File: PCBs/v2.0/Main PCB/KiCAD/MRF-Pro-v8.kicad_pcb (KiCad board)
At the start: 2 copper layers, 56.5 x 28.7 mm, 6 parts, among them J1 Feather-1, J2 Feather-2, J3 FPC 8P Connector, J4 Conn_01x08

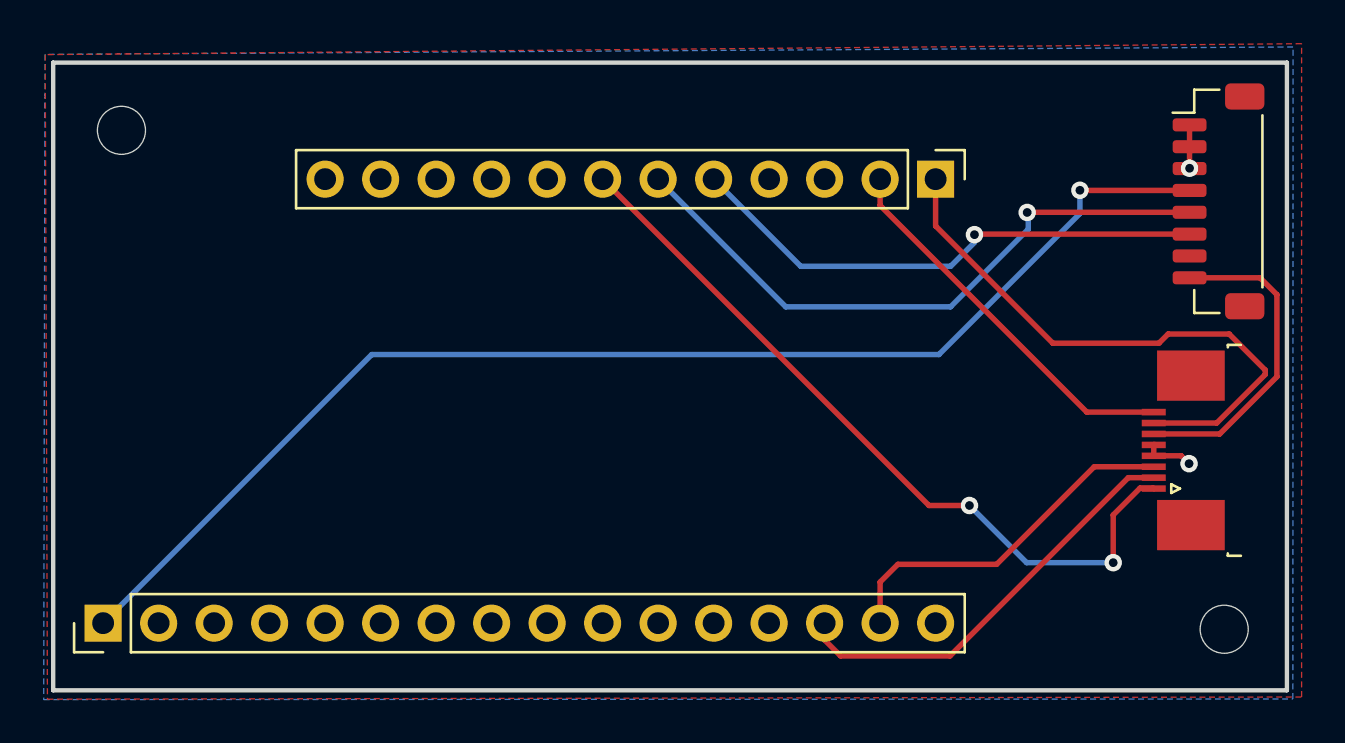
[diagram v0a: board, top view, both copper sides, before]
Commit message: Rework the main-board power switch as a J4 DPDT and lay out the board
The power switch moves onto the 8-pin J4 header as a DPDT: pole A
gates the Feather 3.3V onto the switched rail 3V3_SW (FPC pin 1),
pole B pulls Feather EN to GND when off, holding the MCU off. This
fixes the prior topology where FPC pin 1 ran from a GPIO (D11) and the
Feather 3.3V never reached the FPC. Feather BAT now drives VBAT to FPC
pin 6 for the breakout LDO. Routed to match; D11 and RST are freed.
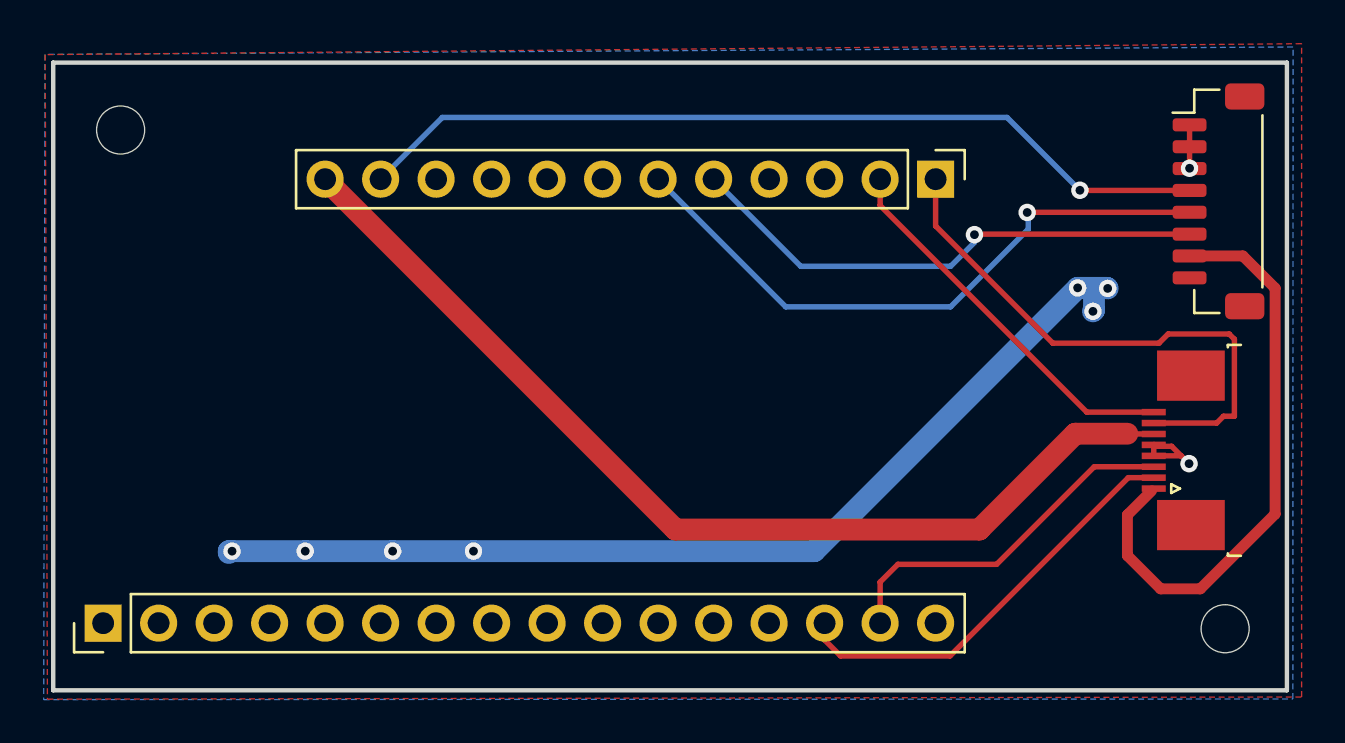
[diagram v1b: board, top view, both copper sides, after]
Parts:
- removed the REF** at (159.3, 122.2)
- removed the REF** at (108.8, 99.4)
- added REF**: MountingHole_2.2mm_M2, MountingHole:MountingHole_2.2mm_M2, F.Cu at (108.8, 99.3)
- added REF**: MountingHole_2.2mm_M2, MountingHole:MountingHole_2.2mm_M2, F.Cu at (159.3, 122.2)
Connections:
- J1 pad 1: Net-(J1-Pin_1) -> unconnected-(J1-Pin_1-Pad1)
- J2 pad 11: unconnected-(J2-Pin_11-Pad11) -> /EN
- J2 pad 12: unconnected-(J2-Pin_12-Pad12) -> /VBAT
- J2 pad 7: Net-(J2-Pin_7) -> unconnected-(J2-Pin_7-Pad7)
- J3 pad 1: Net-(J2-Pin_7) -> /3V3_SW
- J3 pad 6: Net-(J3-Pin_6) -> /VBAT
- J4 pad 4: Net-(J1-Pin_1) -> /EN
- J4 pad 7: /3.3V -> /3V3_SW
- J4 pad 8: Net-(J3-Pin_6) -> /3.3V
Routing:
- net Net-(J1-Pin_1): track 58.6 -> 0.00 mm, vias 1 -> 0
- net /3.3V: track 0.15 -> 46.6 mm, vias 0 -> 7
- net /VBAT: track 0.00 -> 46.4 mm
- net /EN: track 0.00 -> 39.6 mm, vias 0 -> 1
- net Net-(J2-Pin_7): track 35.2 -> 0.00 mm, vias 2 -> 0
- net /3V3_SW: track 0.00 -> 27.1 mm
- net Net-(J3-Pin_6): track 14.8 -> 0.00 mm
- net /GND: track 4.30 -> 5.74 mm
- net Net-(J2-Pin_1): track 26.6 -> 25.8 mm
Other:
- board text added: "MRF2 Daughterboard v8"
- board text removed: "MRF2 Daughterboard v7.5"

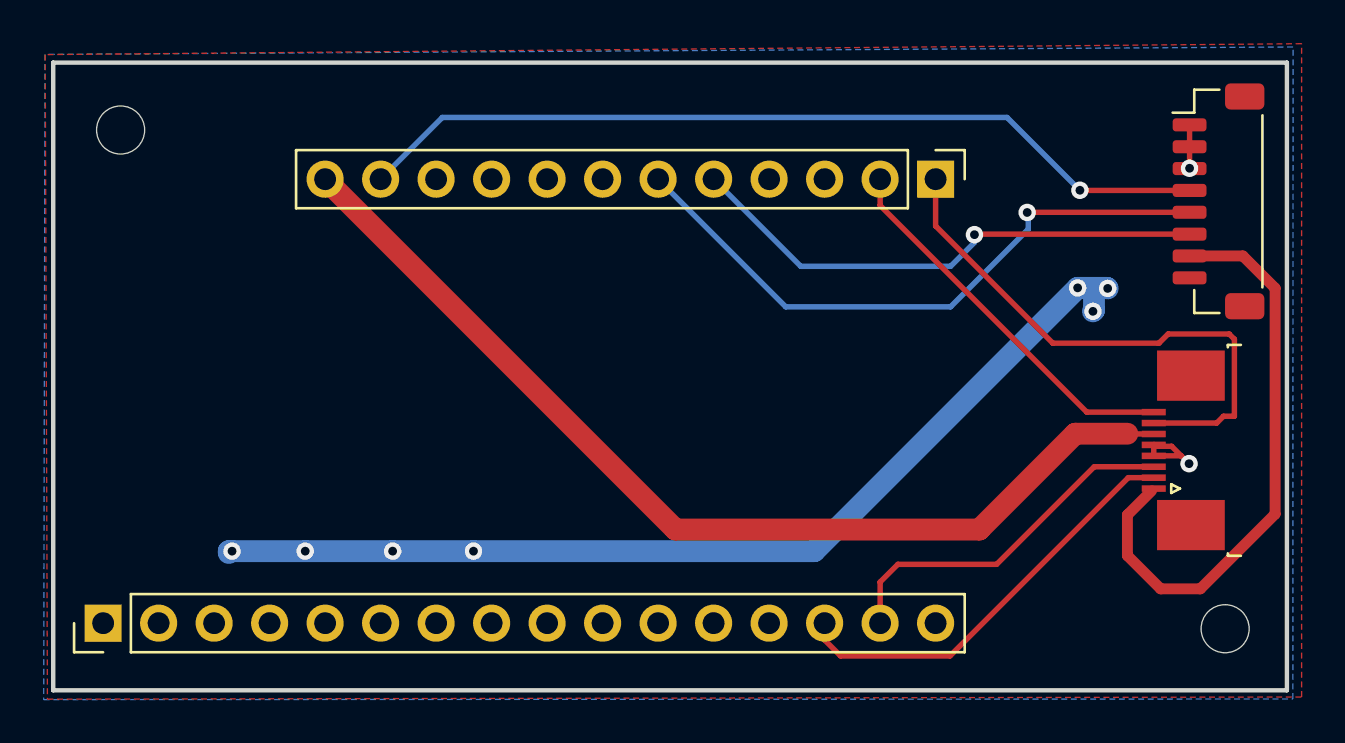
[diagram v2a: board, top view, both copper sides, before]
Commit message: Swap FPC pins 1 and 6, reroute both boards, re-plot fab
VBAT now lands on FPC pin 1 (beside the UART pair) and the switched 3.3 V
on pin 6 (beside the I2C pair), so the always-on battery rail no longer
runs next to the I2C lines. Both boards' schematics were tidied up and
fully rerouted; DRC passes clean on each. Gerbers and the JLCPCB position
files are re-plotted to match. The BOM is unchanged - this is a net and
placement change, not a parts change.
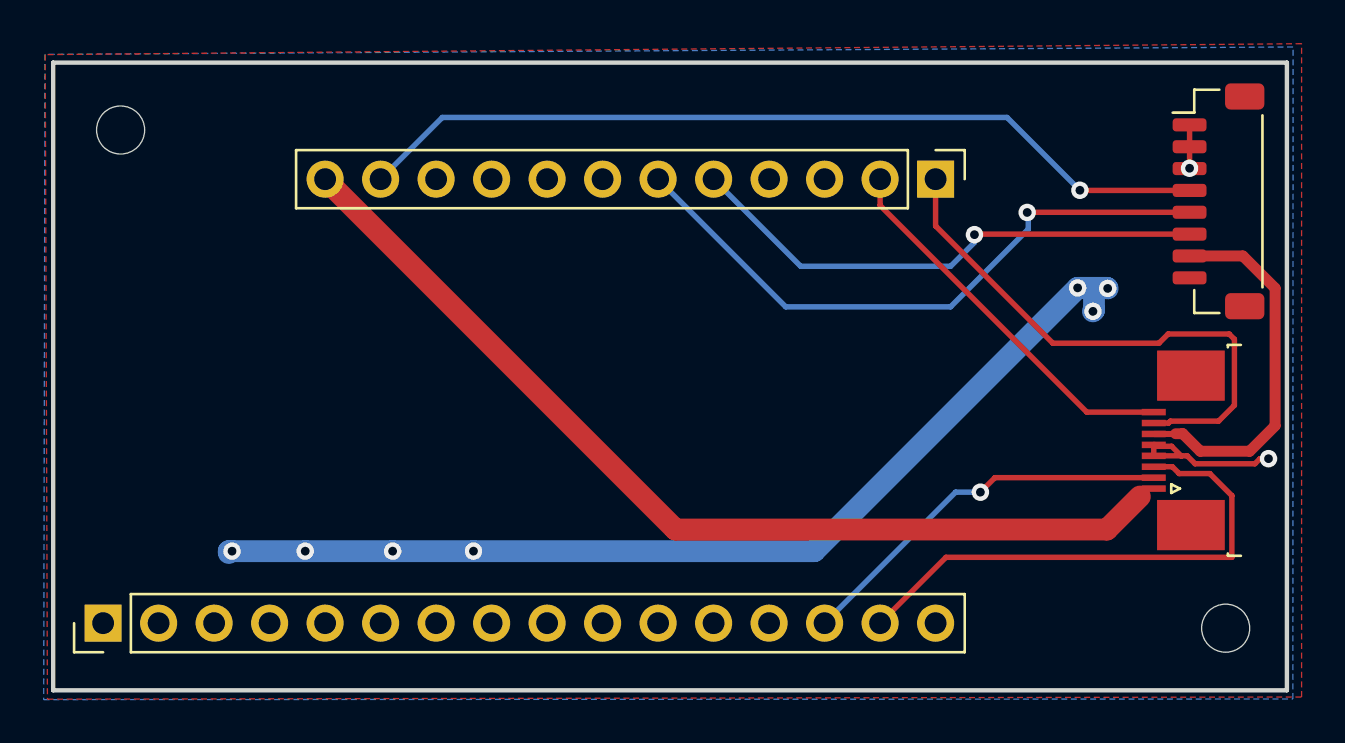
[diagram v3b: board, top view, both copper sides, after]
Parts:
- removed REF** (x2): MountingHole_2.2mm_M2, MountingHole:MountingHole_2.2mm_M2
- added H1: MountingHole, MountingHole:MountingHole_2.2mm_M2, F.Cu at (159.3, 122.2)
- added H2: MountingHole, MountingHole:MountingHole_2.2mm_M2, F.Cu at (108.8, 99.3)
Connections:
- J3 pad 1: /3V3_SW -> /VBAT
- J3 pad 6: /VBAT -> /3V3_SW
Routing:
- net /3V3_SW: track 27.1 -> 17.2 mm
- net Net-(J1-Pin_15): track 16.6 -> 24.3 mm
- net /GND: track 5.74 -> 9.47 mm
- net /VBAT: track 46.4 -> 44.6 mm
- net Net-(J1-Pin_14): track 19.5 -> 17.8 mm, vias 0 -> 1
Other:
- board text added: "SCL SDA 3.3V GND GND RX TX VBAT"
- board text removed: "SCL SDA V+ GND GND RX TX PWM"
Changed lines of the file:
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@@
 	(footprint "MountingHole:MountingHole_2.2mm_M2"
 		(layer "F.Cu")
-		(at 108.75 99.35)
+		(at 159.325 122.15)
 		(descr "Mounting Hole 2.2mm, M2, no annular, generated by kicad-footprint-generator mountinghole.py")
 		(tags "mountinghole M2")
-		(property "Reference" "REF**"
+		(property "Reference" "H1"
 			(at 0 -3.15 0)
 			(layer "F.SilkS")
@@
 			)
 		)
-		(property "Value" "MountingHole_2.2mm_M2"
+		(property "Value" "MountingHole"
 			(at 0 3.15 0)
 			(layer "F.Fab")
@@
 			)
 		)
-		(property "Description" ""
+		(property "Description" "Mounting Hole without connection"
 			(at 0 0 0)
 			(layer "F.Fab")
@@
 			)
 		)
-		(attr exclude_from_pos_files exclude_from_bom)
+		(property ki_fp_filters "MountingHole*")
+		(sheetname "/")
+		(sheetfile "MRF-Pro-v8.kicad_sch")
+		(units
+			(unit
+				(name "A")
+				(pins)
+			)
+		)
+		(attr exclude_from_bom)
 		(duplicate_pad_numbers_are_jumpers no)
 		(fp_circle
@@
 	(footprint "MountingHole:MountingHole_2.2mm_M2"
 		(layer "F.Cu")
-		(at 159.3 122.175)
+		(at 108.75 99.35)
 		(descr "Mounting Hole 2.2mm, M2, no annular, generated by kicad-footprint-generator mountinghole.py")
 		(tags "mountinghole M2")
-		(property "Reference" "REF**"
+		(property "Reference" "H2"
 			(at 0 -3.15 0)
 			(layer "F.SilkS")
@@
 			)
 		)
-		(property "Value" "MountingHole_2.2mm_M2"
+		(property "Value" "MountingHole"
 			(at 0 3.15 0)
 			(layer "F.Fab")
@@
 			)
 		)
-		(property "Description" ""
+		(property "Description" "Mounting Hole without connection"
 			(at 0 0 0)
 			(layer "F.Fab")
@@
 			)
 		)
-		(attr exclude_from_pos_files exclude_from_bom)
+		(property ki_fp_filters "MountingHole*")
+		(sheetname "/")
+		(sheetfile "MRF-Pro-v8.kicad_sch")
+		(units
+			(unit
+				(name "A")
+				(pins)
+			)
+		)
+		(attr exclude_from_bom)
 		(duplicate_pad_numbers_are_jumpers no)
 		(fp_circle
@@
 			(size 0.3 1.1)
 			(layers "F.Cu" "F.Mask" "F.Paste")
-			(net "/3V3_SW")
+			(net "/VBAT")
 			(pinfunction "Pin_1_1")
 			(pintype "passive")
@@
 			(size 0.3 1.1)
 			(layers "F.Cu" "F.Mask" "F.Paste")
-			(net "/VBAT")
+			(net "/3V3_SW")
 			(pinfunction "Pin_6_6")
 			(pintype "passive")
@@
 		(layer "Edge.Cuts")
 	)
-	(gr_text "SCL\nSDA\nV+\nGND\nGND\nRX\nTX\nPWM"
+	(gr_text "SCL\nSDA\n3.3V\nGND\nGND\nRX\nTX\nVBAT"
 		(at 154.6606 118.618 0)
 		(layer "B.SilkS")
@@
 	)
 	(segment
-		(start 158.914 112.7616)
-		(end 159.2256 112.45)
-		(width 0.25)
-		(layer "F.Cu")
-		(net "Net-(J2-Pin_1)")
-	)
-	(segment
 		(start 156.2724 109.1068)
 		(end 156.6926 108.6866)
@@
 	)
 	(segment
-		(start 158.914 112.7616)
-		(end 156.034 112.7616)
-		(width 0.25)
-		(layer "F.Cu")
-		(net "Net-(J2-Pin_1)")
-	)
-	(segment
 		(start 159.725 108.925)
 		(end 159.4866 108.6866)
@@
 	)
 	(segment
-		(start 159.2256 112.45)
-		(end 159.725 112.45)
+		(start 156.709227 112.7616)
+		(end 156.034 112.7616)
 		(width 0.25)
 		(layer "F.Cu")
@@
 	)
 	(segment
-		(start 159.725 112.45)
-		(end 159.725 108.925)
+		(start 159.0006 112.675)
+		(end 156.795827 112.675)
 		(width 0.25)
 		(layer "F.Cu")
@@
 	)
 	(segment
+		(start 159.725 108.925)
+		(end 159.725 111.9506)
+		(width 0.25)
+		(layer "F.Cu")
+		(net "Net-(J2-Pin_1)")
+	)
+	(segment
 		(start 146.05 103.742905)
 		(end 151.413895 109.1068)
@@
 	)
 	(segment
+		(start 159.725 111.9506)
+		(end 159.0006 112.675)
+		(width 0.25)
+		(layer "F.Cu")
+		(net "Net-(J2-Pin_1)")
+	)
+	(segment
 		(start 156.6926 108.6866)
 		(end 159.4866 108.6866)
+		(width 0.25)
+		(layer "F.Cu")
+		(net "Net-(J2-Pin_1)")
+	)
+	(segment
+		(start 156.795827 112.675)
+		(end 156.709227 112.7616)
 		(width 0.25)
 		(layer "F.Cu")
@@
 	)
 	(segment
-		(start 154.825 113.25)
-		(end 152.440235 113.25)
+		(start 134.1452 117.6352)
+		(end 153.8898 117.6352)
 		(width 1)
 		(layer "F.Cu")
@@
 	)
 	(segment
-		(start 156.034 113.2616)
-		(end 154.8366 113.2616)
-		(width 0.25)
+		(start 153.8898 117.6352)
+		(end 155.4 116.125)
+		(width 1)
 		(layer "F.Cu")
 		(net "/VBAT")
 	)
 	(segment
-		(start 156.0224 113.25)
-		(end 156.034 113.2616)
-		(width 0.25)
-		(layer "F.Cu")
-		(net "/VBAT")
-	)
-	(segment
-		(start 134.1452 117.6352)
-		(end 118.11 101.6)
-		(width 1)
-		(layer "F.Cu")
-		(net "/VBAT")
-	)
-	(segment
-		(start 154.8366 113.2616)
-		(end 154.825 113.25)
-		(width 0.25)
-		(layer "F.Cu")
-		(net "/VBAT")
-	)
-	(segment
-		(start 148.055035 117.6352)
+		(start 118.11 101.6)
 		(end 134.1452 117.6352)
 		(width 1)
@@
 	)
 	(segment
-		(start 152.440235 113.25)
-		(end 148.055035 117.6352)
-		(width 1)
-		(layer "F.Cu")
-		(net "/VBAT")
+		(start 160.896454 114.391719)
+		(end 160.663172 114.625)
+		(width 0.25)
+		(layer "F.Cu")
+		(net "/GND")
+	)
+	(segment
+		(start 157.5616 114.2616)
+		(end 157.2916 114.2616)
+		(width 0.25)
+		(layer "F.Cu")
+		(net "/GND")
 	)
 	(segment
@@
 	)
 	(segment
-		(start 157.65 114.62)
-		(end 157.2916 114.2616)
+		(start 160.663172 114.625)
+		(end 157.924999 114.625)
+		(width 0.25)
+		(layer "F.Cu")
+		(net "/GND")
+	)
+	(segment
+		(start 157.924999 114.625)
+		(end 157.5616 114.2616)
+		(width 0.25)
+		(layer "F.Cu")
+		(net "/GND")
+	)
+	(segment
+		(start 161.285364 114.391719)
+		(end 160.896454 114.391719)
 		(width 0.25)
 		(layer "F.Cu")
@@
 	)
 	(via
-		(at 157.65 114.62)
+		(at 161.285364 114.391719)
 		(size 0.8)
 		(drill 0.4)
@@
 	)
 	(segment
-		(start 154.8286 118.8286)
-		(end 156.35 120.35)
+		(start 156.034 113.2616)
+		(end 157.0224 113.2616)
+		(width 0.28)
+		(layer "F.Cu")
+		(net "/3V3_SW")
+	)
+	(segment
+		(start 160.425 114.05)
+		(end 158.163172 114.05)
 		(width 0.5)
 		(layer "F.Cu")
@@
 	)
 	(segment
-		(start 154.8286 116.967)
-		(end 154.8286 118.8286)
+		(start 156.0224 113.25)
+		(end 156.034 113.2616)
+		(width 0.25)
+		(layer "F.Cu")
+		(net "/3V3_SW")
+	)
+	(segment
+		(start 161.5876 112.8874)
+		(end 160.425 114.05)
 		(width 0.5)
 		(layer "F.Cu")
@@
 	)
 	(segment
-		(start 161.5876 116.928)
-		(end 161.5876 106.5876)
+		(start 158.163172 114.05)
+		(end 157.363173 113.25)
 		(width 0.5)
 		(layer "F.Cu")
@@
 	)
 	(segment
-		(start 160.1154 105.1154)
-		(end 157.6728 105.1154)
+		(start 157.0224 113.2616)
+		(end 157.034 113.25)
+		(width 0.25)
+		(layer "F.Cu")
+		(net "/3V3_SW")
+	)
+	(segment
+		(start 157.363173 113.25)
+		(end 157.034 113.25)
 		(width 0.5)
 		(layer "F.Cu")
@@
 	)
 	(segment
-		(start 161.5876 106.5876)
+		(start 157.6728 105.1154)
 		(end 160.1154 105.1154)
 		(width 0.5)
@@
 	)
 	(segment
-		(start 156.35 120.35)
-		(end 158.1656 120.35)
+		(start 161.5876 106.5876)
+		(end 161.5876 112.8874)
 		(width 0.5)
 		(layer "F.Cu")
@@
 	)
 	(segment
-		(start 158.1656 120.35)
-		(end 161.5876 116.928)
-		(width 0.5)
-		(layer "F.Cu")
-		(net "/3V3_SW")
-	)
-	(segment
-		(start 155.934 115.8616)
-		(end 154.8286 116.967)
+		(start 160.1154 105.1154)
+		(end 161.5876 106.5876)
 		(width 0.5)
 		(layer "F.Cu")
@@
 	)
 	(segment
-		(start 140.97 122.69)
-		(end 141.7 123.42)
+		(start 148.7634 115.2616)
+		(end 148.1 115.925)
 		(width 0.25)
 		(layer "F.Cu")
@@
 	)
 	(segment
-		(start 140.97 121.92)
-		(end 140.97 122.69)
+		(start 156.034 115.2616)
+		(end 148.7634 115.2616)
 		(width 0.25)
 		(layer "F.Cu")
 		(net "Net-(J1-Pin_14)")
 	)
-	(segment
-		(start 146.709 123.42)
-		(end 154.8674 115.2616)
-		(width 0.25)
-		(layer "F.Cu")
+	(via
+		(at 148.1 115.925)
+		(size 0.8)
+		(drill 0.4)
+		(layers "F.Cu" "B.Cu")
 		(net "Net-(J1-Pin_14)")
 	)
 	(segment
-		(start 141.7 123.42)
-		(end 146.709 123.42)
-		(width 0.25)
-		(layer "F.Cu")
+		(start 146.965 115.925)
+		(end 140.97 121.92)
+		(width 0.25)
+		(layer "B.Cu")
 		(net "Net-(J1-Pin_14)")
 	)
 	(segment
-		(start 154.8674 115.2616)
-		(end 156.034 115.2616)
-		(width 0.25)
-		(layer "F.Cu")
+		(start 148.1 115.925)
+		(end 146.965 115.925)
+		(width 0.25)
+		(layer "B.Cu")
 		(net "Net-(J1-Pin_14)")
 	)
 	(segment
-		(start 144.3224 119.2276)
-		(end 148.844 119.2276)
+		(start 146.5234 118.9066)
+		(end 159.609 118.9066)
 		(width 0.25)
 		(layer "F.Cu")
@@
 	)
 	(segment
-		(start 143.51 120.04)
-		(end 144.3224 119.2276)
+		(start 143.51 121.92)
+		(end 146.5234 118.9066)
 		(width 0.25)
 		(layer "F.Cu")
@@
 	)
 	(segment
-		(start 143.51 121.92)
-		(end 143.51 120.04)
+		(start 158.6 115.075)
+		(end 157.1974 115.075)
 		(width 0.25)
 		(layer "F.Cu")
@@
 	)
 	(segment
-		(start 153.31 114.7616)
+		(start 156.884 114.7616)
 		(end 156.034 114.7616)
 		(width 0.25)
@@
 	)
 	(segment
-		(start 148.844 119.2276)
-		(end 153.31 114.7616)
-		(width 0.25)
-		(layer "F.Cu")
+		(start 159.609 118.9066)
+		(end 159.609 116.084)
+		(width 0.25)
+		(layer "F.Cu")
+		(net "Net-(J1-Pin_15)")
+	)
+	(segment
+		(start 159.609 116.084)
+		(end 158.6 115.075)
+		(width 0.25)
+		(layer "F.Cu")
+		(net "Net-(J1-Pin_15)")
+	)
+	(segment
+		(start 157.1974 115.075)
+		(end 156.884 114.7616)
+		(width 0.25)
+		(layer "F.Cu")
